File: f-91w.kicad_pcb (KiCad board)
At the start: 4 copper layers, 24.4 x 24.4 mm, 37 parts, among them P10 CONN_01X01, P11 CONN_01X01, P13 CONN_01X01, P14 CONN_01X01, P5 CONN_01X01, P6 CONN_01X01, P7 CONN_01X01, P8 CONN_01X01, P9 CONN_01X01, Q1 BC846, U1 CY8C4248LQI-BL483, U2 LCD-F-91W, U3 BME680, Y1 32.768KHz, Y2 24MHz

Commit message: More routing
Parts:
- moved C5 0.16 mm to (53.5, 100.4)
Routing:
- net VDDR: track 9.69 -> 18.2 mm, vias 1 -> 4
- net GND: track 9.33 -> 16.5 mm, vias 10 -> 22
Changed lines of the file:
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@@
   (general
     (links 102)
-    (no_connects 68)
+    (no_connects 29)
     (area 45.663181 84.883147 70.163247 109.362848)
     (thickness 0.6)
     (drawings 508)
-    (tracks 317)
+    (tracks 371)
     (zones 0)
     (modules 37)
@@
     (1 In1.Cu power hide)
     (2 In2.Cu signal hide)
-    (31 B.Cu signal hide)
+    (31 B.Cu signal)
     (32 B.Adhes user hide)
     (33 F.Adhes user)
@@
     (38 B.Mask user)
     (39 F.Mask user)
-    (40 Dwgs.User user)
+    (40 Dwgs.User user hide)
     (41 Cmts.User user)
     (42 Eco1.User user)
     (43 Eco2.User user hide)
-    (44 Edge.Cuts user hide)
+    (44 Edge.Cuts user)
     (45 Margin user)
     (46 B.CrtYd user hide)
     (47 F.CrtYd user)
-    (48 B.Fab user)
+    (48 B.Fab user hide)
     (49 F.Fab user hide)
   )
@@
   )
   (module Capacitors_SMD:C_0201_NoSilk (layer F.Cu)
-    (at 53.6555 100.391 270)
+    (at 53.5 100.391 270)
     (descr "Capacitor SMD 0201, reflow soldering, AVX (see smccp.pdf)")
     (tags "capacitor 0201")
@@
   (segment (start 55.8 102.9) (end 55.2555 103.4445) (width 0.127) (layer F.Cu) (net 1))
   (segment (start 55.2465 103.9) (end 55.2555 103.891) (width 0.127) (layer F.Cu) (net 1))
+  (segment (start 57.7 104.48) (end 58.1445 104.48) (width 0.2) (layer F.Cu) (net 2))
+  (segment (start 58.1445 104.48) (end 58.2555 104.591) (width 0.2) (layer F.Cu) (net 2))
+  (via (at 58.2555 104.591) (size 0.35) (drill 0.2) (layers F.Cu B.Cu) (net 2))
+  (segment (start 57.7 104.48) (end 57.7 105.0465) (width 0.2) (layer F.Cu) (net 2))
+  (segment (start 57.7 105.0465) (end 57.6555 105.091) (width 0.2) (layer F.Cu) (net 2))
+  (via (at 57.6555 105.091) (size 0.35) (drill 0.2) (layers F.Cu B.Cu) (net 2))
+  (segment (start 54.2 104.58) (end 53.6665 104.58) (width 0.2) (layer F.Cu) (net 2))
+  (segment (start 53.6665 104.58) (end 53.6555 104.591) (width 0.2) (layer F.Cu) (net 2))
+  (via (at 53.6555 104.591) (size 0.35) (drill 0.2) (layers F.Cu B.Cu) (net 2))
+  (segment (start 54.2 104.58) (end 54.2 105.0465) (width 0.2) (layer F.Cu) (net 2))
+  (segment (start 54.2 105.0465) (end 54.1555 105.091) (width 0.2) (layer F.Cu) (net 2))
+  (via (at 54.1555 105.091) (size 0.35) (drill 0.2) (layers F.Cu B.Cu) (net 2))
+  (segment (start 50.9 103.55) (end 50.9 104.0465) (width 0.2) (layer F.Cu) (net 2))
+  (segment (start 50.9 104.0465) (end 50.7555 104.191) (width 0.2) (layer F.Cu) (net 2))
+  (via (at 50.7555 104.191) (size 0.35) (drill 0.2) (layers F.Cu B.Cu) (net 2))
+  (segment (start 50.409 103.591) (end 50.2555 103.591) (width 0.2) (layer F.Cu) (net 2))
+  (via (at 50.2555 103.591) (size 0.35) (drill 0.2) (layers F.Cu B.Cu) (net 2))
+  (segment (start 50.9 103.55) (end 50.45 103.55) (width 0.2) (layer F.Cu) (net 2))
+  (segment (start 50.45 103.55) (end 50.409 103.591) (width 0.2) (layer F.Cu) (net 2))
+  (segment (start 53.6555 100.111) (end 53.0755 100.111) (width 0.2) (layer F.Cu) (net 2))
+  (segment (start 53.0755 100.111) (end 53.0555 100.091) (width 0.2) (layer F.Cu) (net 2))
+  (via (at 52.9 100.091) (size 0.35) (drill 0.2) (layers F.Cu B.Cu) (net 2))
+  (via (at 54.7755 101.811) (size 0.35) (drill 0.2) (layers F.Cu B.Cu) (net 2))
+  (segment (start 54.7755 102.391) (end 54.7755 101.811) (width 0.2) (layer F.Cu) (net 2))
+  (segment (start 58.9 102.971) (end 58.9 103.4465) (width 0.2) (layer F.Cu) (net 2))
+  (segment (start 58.9 103.4465) (end 58.8555 103.491) (width 0.2) (layer F.Cu) (net 2))
+  (via (at 58.8555 103.491) (size 0.35) (drill 0.2) (layers F.Cu B.Cu) (net 2))
+  (via (at 58.3755 102.971) (size 0.35) (drill 0.2) (layers F.Cu B.Cu) (net 2))
+  (segment (start 58.9 102.971) (end 58.3755 102.971) (width 0.2) (layer F.Cu) (net 2))
+  (segment (start 60.7 102.971) (end 60.7 103.4355) (width 0.2) (layer F.Cu) (net 2))
+  (segment (start 60.7 103.4355) (end 60.7555 103.491) (width 0.2) (layer F.Cu) (net 2))
+  (via (at 60.7555 103.491) (size 0.35) (drill 0.2) (layers F.Cu B.Cu) (net 2))
+  (segment (start 61.1755 102.971) (end 61.2555 102.891) (width 0.2) (layer F.Cu) (net 2))
+  (segment (start 61.2555 102.891) (end 61.3555 102.891) (width 0.2) (layer F.Cu) (net 2))
+  (via (at 61.3555 102.891) (size 0.35) (drill 0.2) (layers F.Cu B.Cu) (net 2))
+  (segment (start 60.7 102.971) (end 61.1755 102.971) (width 0.2) (layer F.Cu) (net 2))
   (segment (start 64.541 102.391) (end 64.6555 102.391) (width 0.2) (layer F.Cu) (net 2))
   (via (at 64.6555 102.391) (size 0.35) (drill 0.2) (layers F.Cu B.Cu) (net 2))
@@
   (segment (start 56.2 102.9) (end 56.6555 103.3555) (width 0.127) (layer F.Cu) (net 40))
   (segment (start 59.8 104) (end 59.8 101.385) (width 0.127) (layer F.Cu) (net 42))
-  (segment (start 53.6555 100.671) (end 54.544 100.671) (width 0.127) (layer F.Cu) (net 43))
-  (segment (start 54.544 100.671) (end 54.615 100.6) (width 0.127) (layer F.Cu) (net 43))
+  (segment (start 54.615 100.6) (end 53.7265 100.6) (width 0.127) (layer F.Cu) (net 43))
+  (segment (start 53.7265 100.6) (end 53.6555 100.671) (width 0.127) (layer F.Cu) (net 43))
+  (segment (start 62.0555 101.391) (end 62.0555 101.5055) (width 0.2) (layer F.Cu) (net 44))
+  (segment (start 62.0555 101.5055) (end 62.65 102.1) (width 0.2) (layer F.Cu) (net 44))
+  (segment (start 62.0555 99.682987) (end 62.0555 101.391) (width 0.2) (layer B.Cu) (net 44))
+  (via (at 62.0555 101.391) (size 0.35) (drill 0.2) (layers F.Cu B.Cu) (net 44))
+  (segment (start 62.1 99.391) (end 62.1 99.638487) (width 0.2) (layer B.Cu) (net 44))
+  (segment (start 62.1 99.638487) (end 62.0555 99.682987) (width 0.2) (layer B.Cu) (net 44))
+  (segment (start 61.6555 102) (end 61.1645 102.491) (width 0.2) (layer B.Cu) (net 44))
+  (segment (start 61.1645 102.491) (end 60.9555 102.491) (width 0.2) (layer B.Cu) (net 44))
+  (segment (start 61.6555 102) (end 62.55 102) (width 0.2) (layer F.Cu) (net 44))
+  (segment (start 62.55 102) (end 62.65 102.1) (width 0.2) (layer F.Cu) (net 44))
+  (segment (start 62.65 102.1) (end 62.65 101.65) (width 0.2) (layer F.Cu) (net 44))
+  (via (at 61.6555 102) (size 0.35) (drill 0.2) (layers F.Cu B.Cu) (net 44))
+  (segment (start 58.3555 102.491) (end 60.9555 102.491) (width 0.2) (layer B.Cu) (net 44))
+  (segment (start 58.4555 102.4805) (end 58.366 102.4805) (width 0.2) (layer F.Cu) (net 44))
+  (segment (start 58.366 102.4805) (end 58.3555 102.491) (width 0.2) (layer F.Cu) (net 44))
+  (via (at 58.3555 102.491) (size 0.35) (drill 0.2) (layers F.Cu B.Cu) (net 44))
+  (segment (start 58.9 102.411) (end 58.525 102.411) (width 0.2) (layer F.Cu) (net 44))
+  (segment (start 58.525 102.411) (end 58.4555 102.4805) (width 0.2) (layer F.Cu) (net 44))
   (segment (start 62.65 102.835) (end 62.89 102.835) (width 0.2) (layer F.Cu) (net 44))
   (segment (start 62.89 102.835) (end 62.94 102.885) (width 0.2) (layer F.Cu) (net 44))

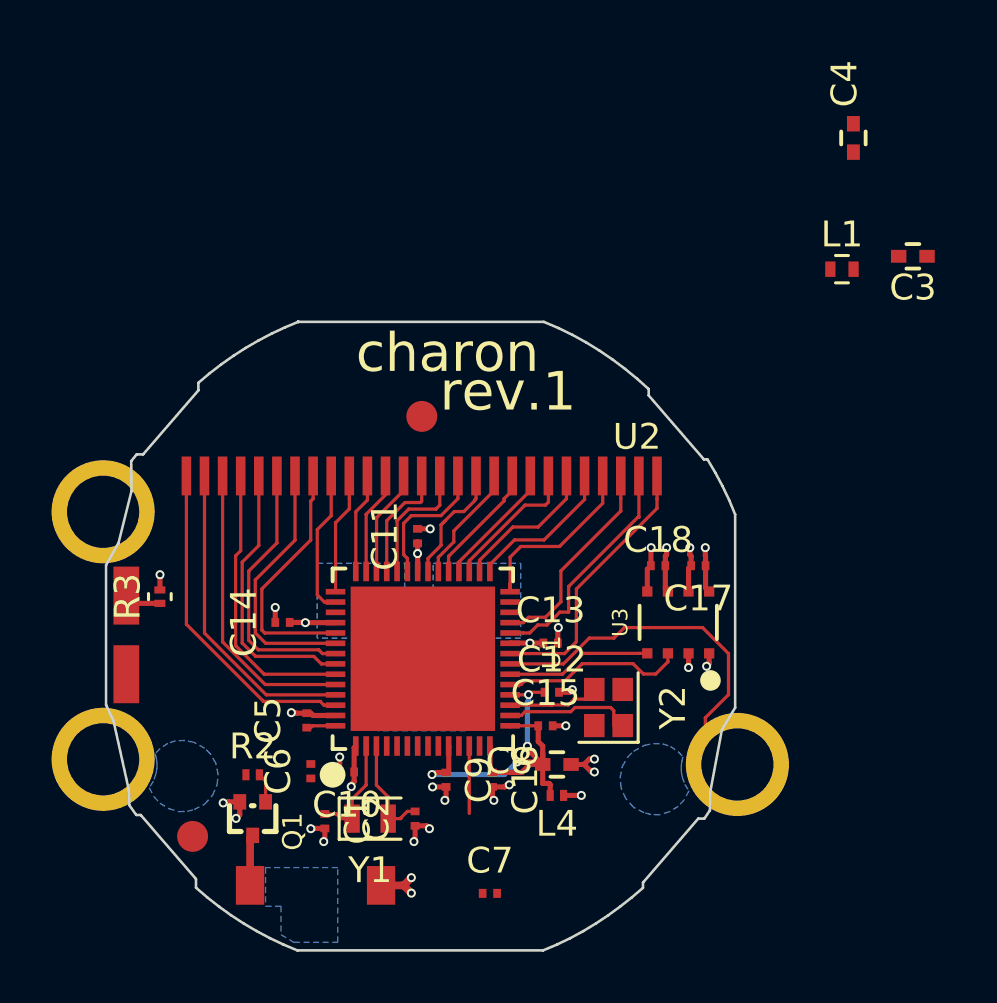
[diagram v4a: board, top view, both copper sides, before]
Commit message: Add back in accidentally deleted mechanical holes
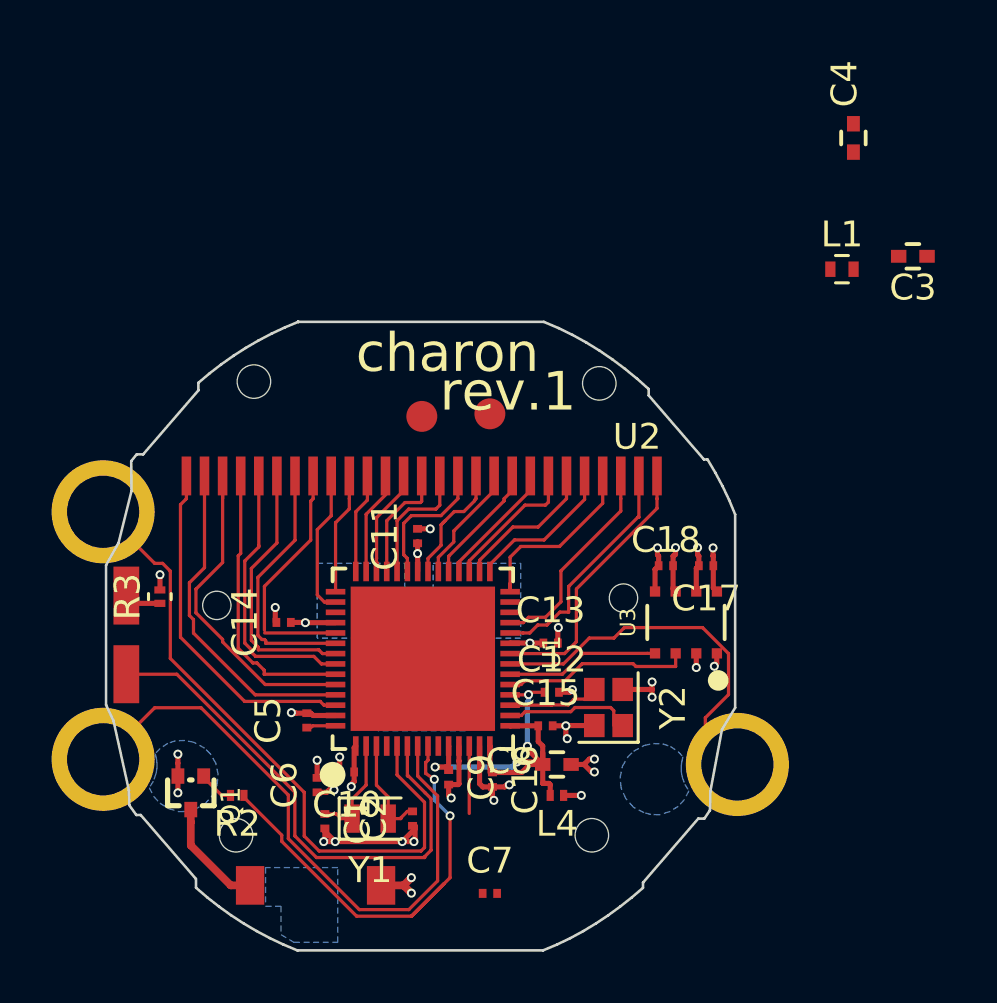
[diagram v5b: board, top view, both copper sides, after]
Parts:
- added REF**: HOLE_1.1MM, f-91w:HOLE_1.1MM, F.Cu at (50.0, 95.9)
- added REF**: HOLE_1.1MM, f-91w:HOLE_1.1MM, F.Cu at (65.8, 95.6)
- added REF**: HOLE_1.3MM, f-91w:HOLE_1.3MM, F.Cu at (51.4, 87.2)
- added REF**: HOLE_1.3MM, f-91w:HOLE_1.3MM, F.Cu at (64.4, 87.3)
- added REF**: HOLE_1.3MM, f-91w:HOLE_1.3MM, F.Cu at (50.8, 104.8)
- added REF**: HOLE_1.3MM, f-91w:HOLE_1.3MM, F.Cu at (64.6, 104.8)
- moved P14 20.0 mm to (60.6, 88.5)
- moved Q1 2.60 mm to (49.0, 103.2)
- moved R2 1.00 mm to (50.8, 103.3), turned to 180 degrees
- moved C6 0.59 mm to (53.9, 102.9)
- moved C17 0.30 mm to (69.0, 94.4)
- moved C18 0.30 mm to (67.4, 94.4)
- moved U3 0.30 mm to (68.2, 96.6)
- moved C9 0.14 mm to (59.0, 102.6)
- moved C2 0.10 mm to (57.6, 104.2)
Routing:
- net /B_LIGHT: track 0.00 -> 25.3 mm
- net /B_MODE: track 0.00 -> 24.0 mm
- net /LED_1: track 0.00 -> 20.3 mm
- net /BUZ_EN: track 0.00 -> 20.0 mm, vias 0 -> 2
- net GND: track 16.5 -> 27.8 mm, vias 22 -> 25
- net /BUZ: track 2.05 -> 4.40 mm
- net /LCD_SEG3: track 11.5 -> 13.2 mm
- net /LCD_SEG2: track 12.2 -> 12.9 mm
- net VCC: track 13.0 -> 13.6 mm, vias 11 -> 12
- net /LCD_SEG1: track 12.8 -> 13.5 mm

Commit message: Add Johanson 2450AT42E0100 antenna, initial placement
TODO: Proper ground plane and 50R trace
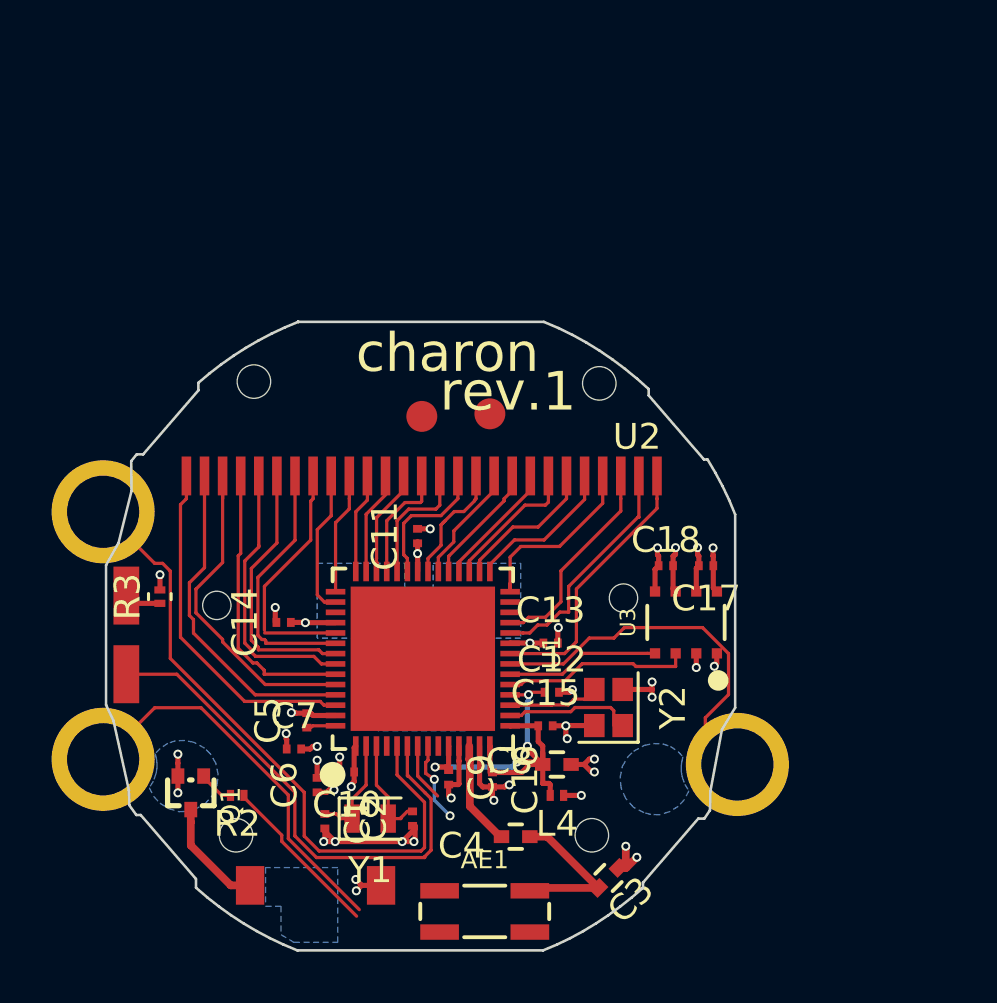
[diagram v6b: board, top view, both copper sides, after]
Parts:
- removed L1: L_Small, Resistors_SMD:R_0402
- added AE1: TBD, f-91w:2450AT42E0100, F.Cu at (60.4, 107.8)
- moved C4 30.1 mm to (61.6, 104.9), turned to 0 degrees
- moved C3 26.8 mm to (65.2, 106.5), turned to 45 degrees
- moved C7 9.44 mm to (53.0, 101.5)
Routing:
- net /BUZ_EN: track 20.0 -> 9.76 mm
- net /B_MODE: track 24.0 -> 17.3 mm
- net Net-(AE1-Pad1): track 0.00 -> 6.19 mm
- net GND: track 27.8 -> 30.3 mm, vias 25 -> 28
- net Net-(C4-Pad1): track 2.61 -> 4.06 mm
- net VCC: track 13.6 -> 13.9 mm, vias 12 -> 13

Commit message: Add test points for SWD interface
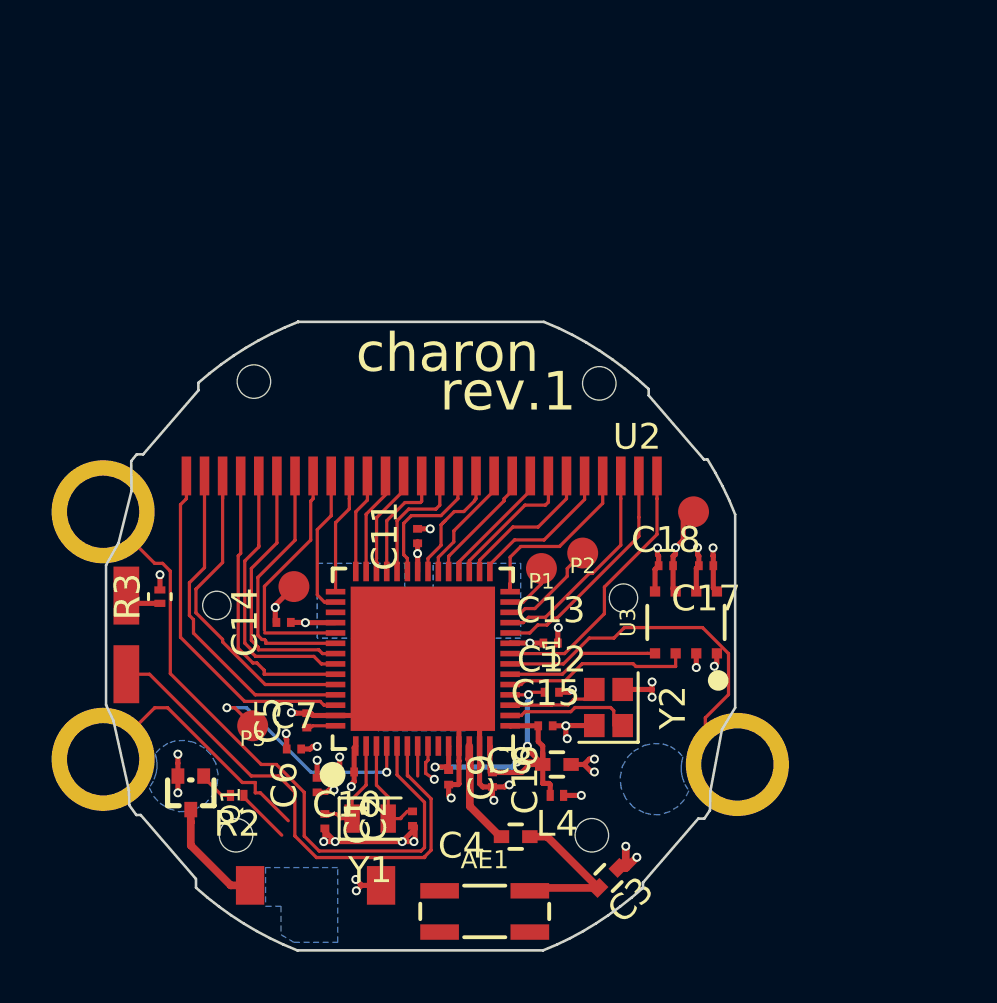
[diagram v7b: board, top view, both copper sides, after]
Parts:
- added P1: CONN_01X01, f-91w:TP_1.2mm, F.Cu at (62.6, 94.5)
- added P2: CONN_01X01, f-91w:TP_1.2mm, F.Cu at (64.2, 93.9)
- added P3: CONN_01X01, f-91w:TP_1.2mm, F.Cu at (51.4, 100.6)
- moved P14 8.77 mm to (68.5, 92.3)
- moved P13 8.26 mm to (53.0, 95.2)
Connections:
- U1 pad 26: (no net) -> /SWDIO
- U1 pad 27: (no net) -> /SWCLK
- U1 pad 4: (no net) -> //XRES
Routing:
- net GND: track 30.3 -> 44.0 mm
- net //XRES: track 0.00 -> 9.54 mm, vias 0 -> 2
- net /B_MODE: track 17.3 -> 11.2 mm
- net /BUZ_EN: track 9.76 -> 3.75 mm, vias 2 -> 1
- net /SWDIO: track 0.00 -> 3.94 mm
- net /SWCLK: track 0.00 -> 2.00 mm
- net VCC: track 13.9 -> 15.8 mm
